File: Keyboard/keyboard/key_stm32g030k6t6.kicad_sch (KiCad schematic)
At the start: 9 parts, among them J1 Conn_01x06_Male, J2 Conn_01x06_Male, SW1 SW_Push, U1 STM32G030K6T6

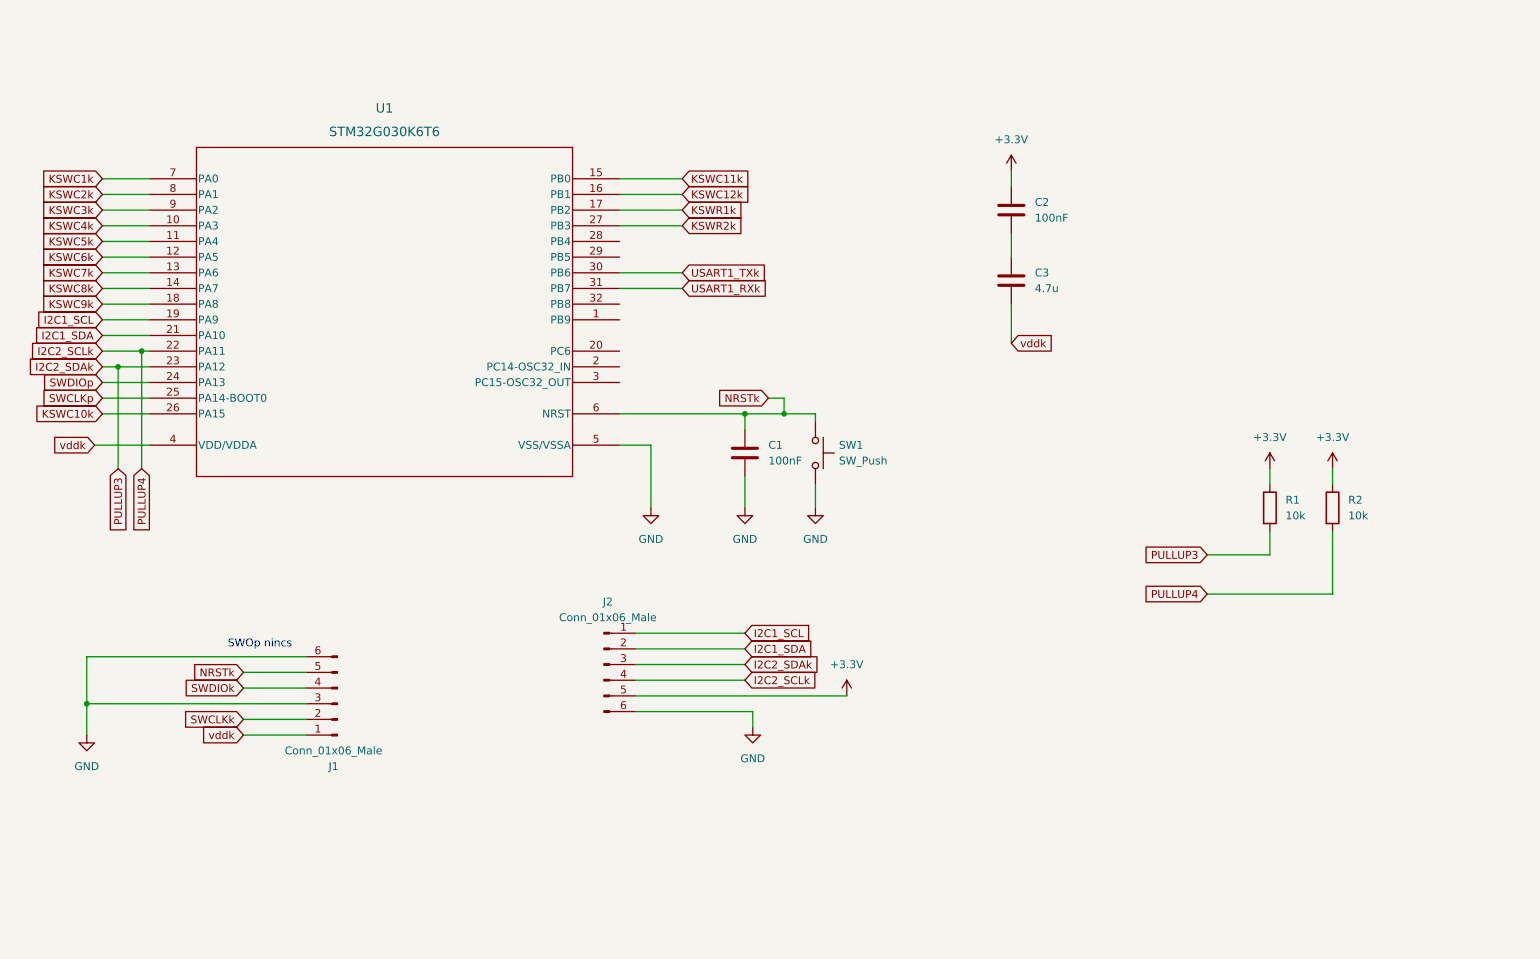
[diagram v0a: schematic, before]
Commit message: fixing keyboard and pot project schematics
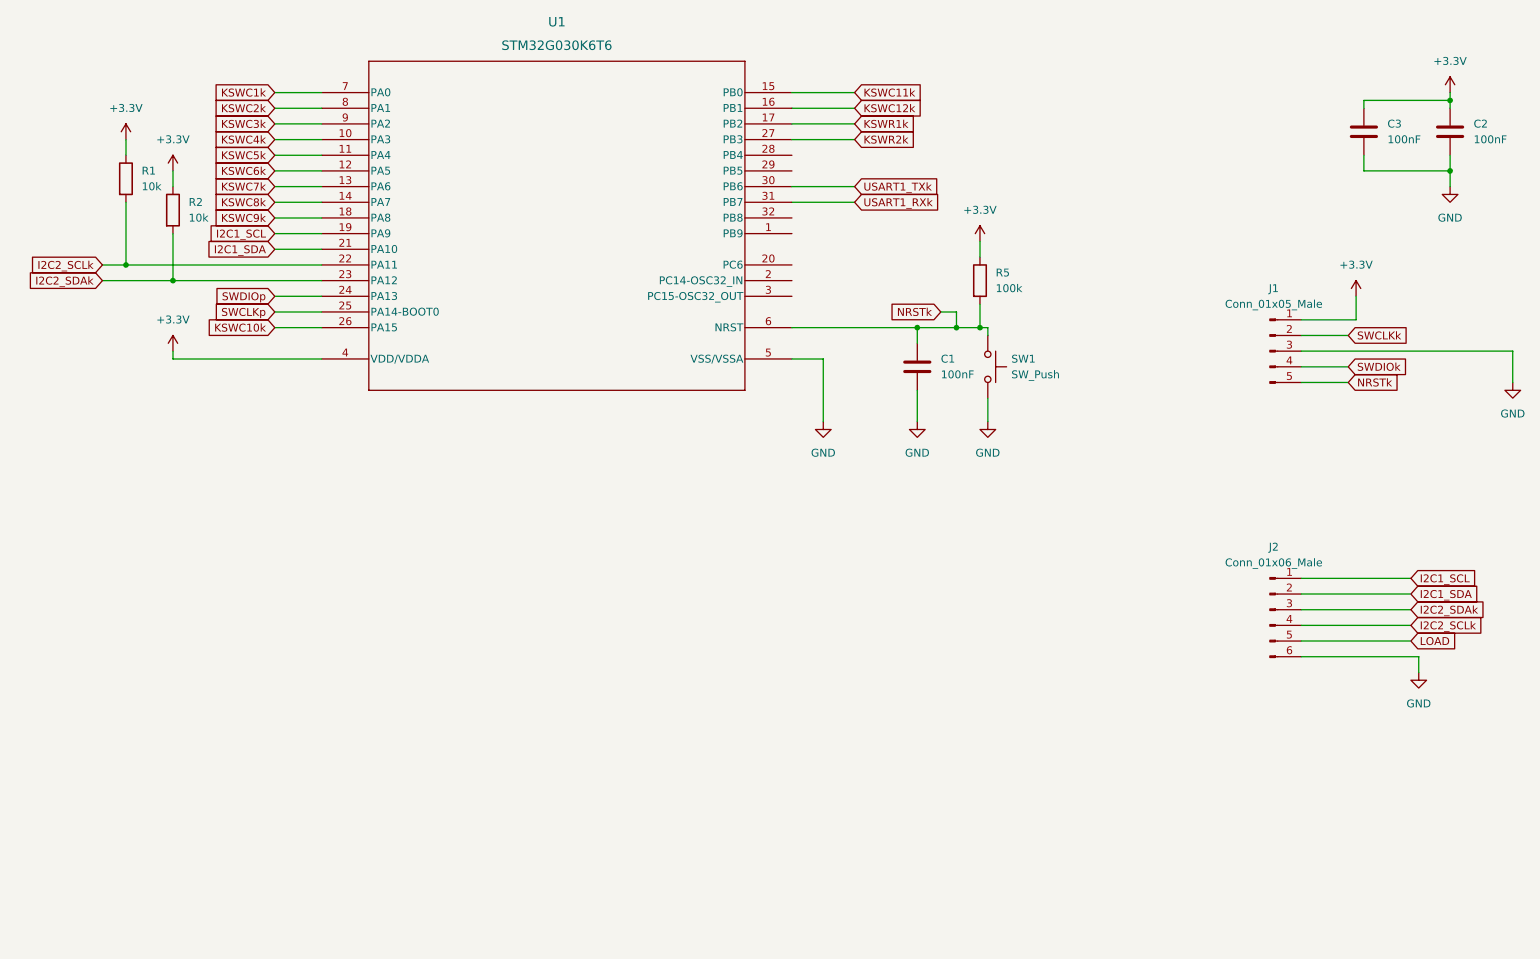
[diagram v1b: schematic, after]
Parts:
- removed J1: Conn_01x06_Male, Connector_PinSocket_2.54mm:PinSocket_1x06_P2.54mm_Horizontal, symbol Connector:Conn_01x06_Male
- added J1: Conn_01x05_Male, symbol Connector:Conn_01x05_Male
- added R5: 100k, Resistor_SMD:R_0805_2012Metric_Pad1.20x1.40mm_HandSolder, symbol Device:R
- C3: value 4.7u -> 100nF
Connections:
- net +3V3: now also C3.1, U1.4 (VDD/VDDA), J1.1 (Pin_1), R5.1; no longer J2.5 (Pin_5)
- net GND: now also C2.2, C3.2, J1.3 (Pin_3)
- net I2C2_SCLk: now also R1.2; no longer R2.2
- net I2C2_SDAk: now also R2.2; no longer R1.2
- net NRSTk: now also J1.5 (Pin_5), R5.2
- net SWCLKk: now also J1.2 (Pin_2)
- net SWDIOk: now also J1.4 (Pin_4)
- removed net vddk: C3.2, U1.4 (VDD/VDDA)
- new net LOAD: J2.5 (Pin_5)
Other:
- note removed: "SWOp nincs"
- moved on the sheet: C1, C2, J2, R1, R2, SW1, U1

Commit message: main_func pcb done
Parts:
- added D14: GREEN LED, LED_SMD:LED_0805_2012Metric_Pad1.15x1.40mm_HandSolder, symbol Device:LED
- added D15: RED LED, LED_SMD:LED_0805_2012Metric_Pad1.15x1.40mm_HandSolder, symbol Device:LED
- added R10, R9: 1k, Resistor_SMD:R_0805_2012Metric_Pad1.20x1.40mm_HandSolder, symbol Device:R
- J1: footprint (none) -> Connector_PinSocket_2.54mm:PinSocket_1x05_P2.54mm_Horizontal
- J2: footprint (none) -> Connector_PinSocket_2.54mm:PinSocket_1x06_P2.54mm_Horizontal
- SW1: footprint (none) -> tactile_button:ROCPU Switches TP10721645
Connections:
- net +3V3: now also D14.2 (A)
- net GND: now also D15.1 (K)
- net USART1_TXk: now also R10.1, R9.1
- new net: D14.1 (K), R9.2
- new net: D15.2 (A), R10.2
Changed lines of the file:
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@@
   (junction (at 173.99 76.2) (diameter 0) (color 0 0 0 0)
   )
+  (junction (at 179.07 113.03) (diameter 0) (color 0 0 0 0)
+  )
   (junction (at 260.35 39.37) (diameter 0) (color 0 0 0 0)
   )
@@
     (stroke (width 0) (type default) (color 0 0 0 0))
   )
+  (wire (pts (xy 179.07 113.03) (xy 161.29 113.03))
+    (stroke (width 0) (type default) (color 0 0 0 0))
+  )
   (wire (pts (xy 173.99 78.74) (xy 173.99 76.2))
     (stroke (width 0) (type default) (color 0 0 0 0))
@@
     (stroke (width 0) (type default) (color 0 0 0 0))
   )
+  (wire (pts (xy 179.07 113.03) (xy 179.07 116.84))
+    (stroke (width 0) (type default) (color 0 0 0 0))
+  )
   (wire (pts (xy 45.72 45.72) (xy 45.72 48.26))
     (stroke (width 0) (type default) (color 0 0 0 0))
   )
+  (wire (pts (xy 179.07 124.46) (xy 179.07 129.54))
+    (stroke (width 0) (type default) (color 0 0 0 0))
+  )
   (wire (pts (xy 180.34 76.2) (xy 173.99 76.2))
     (stroke (width 0) (type default) (color 0 0 0 0))
@@
     (stroke (width 0) (type default) (color 0 0 0 0))
   )
+  (wire (pts (xy 186.69 113.03) (xy 179.07 113.03))
+    (stroke (width 0) (type default) (color 0 0 0 0))
+  )
   (wire (pts (xy 236.22 121.92) (xy 254 121.92))
     (stroke (width 0) (type default) (color 0 0 0 0))
@@
     (stroke (width 0) (type default) (color 0 0 0 0))
   )
+  (wire (pts (xy 156.21 146.05) (xy 161.29 146.05))
+    (stroke (width 0) (type default) (color 0 0 0 0))
+  )
   (wire (pts (xy 246.38 48.26) (xy 246.38 50.8))
     (stroke (width 0) (type default) (color 0 0 0 0))
@@
     (stroke (width 0) (type default) (color 0 0 0 0))
   )
+  (wire (pts (xy 161.29 113.03) (xy 161.29 116.84))
+    (stroke (width 0) (type default) (color 0 0 0 0))
+  )
   (wire (pts (xy 69.85 45.72) (xy 77.47 45.72))
     (stroke (width 0) (type default) (color 0 0 0 0))
@@
     (stroke (width 0) (type default) (color 0 0 0 0))
   )
+  (wire (pts (xy 179.07 137.16) (xy 179.07 144.78))
+    (stroke (width 0) (type default) (color 0 0 0 0))
+  )
   (wire (pts (xy 236.22 124.46) (xy 254 124.46))
     (stroke (width 0) (type default) (color 0 0 0 0))
@@
     (stroke (width 0) (type default) (color 0 0 0 0))
   )
+  (wire (pts (xy 156.21 143.51) (xy 156.21 146.05))
+    (stroke (width 0) (type default) (color 0 0 0 0))
+  )
   (wire (pts (xy 153.67 38.1) (xy 163.83 38.1))
     (stroke (width 0) (type default) (color 0 0 0 0))
@@
     (stroke (width 0) (type default) (color 0 0 0 0))
   )
+  (wire (pts (xy 161.29 124.46) (xy 161.29 129.54))
+    (stroke (width 0) (type default) (color 0 0 0 0))
+  )
   (wire (pts (xy 260.35 48.26) (xy 260.35 50.8))
     (stroke (width 0) (type default) (color 0 0 0 0))
@@
     (stroke (width 0) (type default) (color 0 0 0 0))
   )
+  (wire (pts (xy 161.29 146.05) (xy 161.29 137.16))
+    (stroke (width 0) (type default) (color 0 0 0 0))
+  )
   (wire (pts (xy 41.91 68.58) (xy 53.34 68.58))
     (stroke (width 0) (type default) (color 0 0 0 0))
@@
     (property "Intersheet References" "${INTERSHEET_REFS}" (id 0) (at 59.9983 38.0206 0)
       (effects (font (size 1.27 1.27)) (justify right) hide)
+    )
+  )
+  (global_label "USART1_TXk" (shape input) (at 186.69 113.03 0) (fields_autoplaced)
+    (effects (font (size 1.27 1.27)) (justify left))
+    (property "Intersheet References" "${INTERSHEET_REFS}" (id 0) (at 200.3517 112.9506 0)
+      (effects (font (size 1.27 1.27)) (justify left) hide)
     )
   )
@@
     (pin "1")
   )
+  (symbol (lib_id "Device:R") (at 161.29 120.65 0) (unit 1)
+    (in_bom yes) (on_board yes) (fields_autoplaced)
+    (property "Reference" "R9" (id 0) (at 163.83 119.3799 0)
+      (effects (font (size 1.27 1.27)) (justify left))
+    )
+    (property "Value" "1k" (id 1) (at 163.83 121.9199 0)
+      (effects (font (size 1.27 1.27)) (justify left))
+    )
+    (property "Footprint" "Resistor_SMD:R_0805_2012Metric_Pad1.20x1.40mm_HandSolder" (id 2) (at 159.512 120.65 90)
+      (effects (font (size 1.27 1.27)) hide)
+    )
+    (property "Datasheet" "~" (id 3) (at 161.29 120.65 0)
+      (effects (font (size 1.27 1.27)) hide)
+    )
+    (pin "1")
+    (pin "2")
+  )
   (symbol (lib_id "power:GND") (at 255.27 132.08 0) (unit 1)
     (in_bom yes) (on_board yes) (fields_autoplaced)
@@
     (pin "1")
   )
+  (symbol (lib_id "Device:R") (at 179.07 120.65 0) (unit 1)
+    (in_bom yes) (on_board yes) (fields_autoplaced)
+    (property "Reference" "R10" (id 0) (at 181.61 119.3799 0)
+      (effects (font (size 1.27 1.27)) (justify left))
+    )
+    (property "Value" "1k" (id 1) (at 181.61 121.9199 0)
+      (effects (font (size 1.27 1.27)) (justify left))
+    )
+    (property "Footprint" "Resistor_SMD:R_0805_2012Metric_Pad1.20x1.40mm_HandSolder" (id 2) (at 177.292 120.65 90)
+      (effects (font (size 1.27 1.27)) hide)
+    )
+    (property "Datasheet" "~" (id 3) (at 179.07 120.65 0)
+      (effects (font (size 1.27 1.27)) hide)
+    )
+    (pin "1")
+    (pin "2")
+  )
   (symbol (lib_id "Device:R") (at 53.34 57.15 0) (unit 1)
     (in_bom yes) (on_board yes) (fields_autoplaced)
@@
     (property "Reference" "J2" (id 0) (at 231.775 111.76 0))
     (property "Value" "Conn_01x06_Male" (id 1) (at 231.775 114.3 0))
-    (property "Footprint" "" (id 2) (at 231.14 121.92 0)
+    (property "Footprint" "Connector_PinSocket_2.54mm:PinSocket_1x06_P2.54mm_Horizontal" (id 2) (at 231.14 121.92 0)
       (effects (font (size 1.27 1.27)) hide)
     )
@@
     (pin "1")
   )
+  (symbol (lib_id "power:+3.3V") (at 156.21 143.51 0) (unit 1)
+    (in_bom yes) (on_board yes) (fields_autoplaced)
+    (property "Reference" "#PWR016" (id 0) (at 156.21 147.32 0)
+      (effects (font (size 1.27 1.27)) hide)
+    )
+    (property "Value" "+3.3V" (id 1) (at 156.21 138.43 0))
+    (property "Footprint" "" (id 2) (at 156.21 143.51 0)
+      (effects (font (size 1.27 1.27)) hide)
+    )
+    (property "Datasheet" "" (id 3) (at 156.21 143.51 0)
+      (effects (font (size 1.27 1.27)) hide)
+    )
+    (pin "1")
+  )
   (symbol (lib_id "power:+3.3V") (at 53.34 50.8 0) (unit 1)
     (in_bom yes) (on_board yes) (fields_autoplaced)
@@
     (pin "1")
   )
+  (symbol (lib_id "Device:LED") (at 179.07 133.35 90) (unit 1)
+    (in_bom yes) (on_board yes) (fields_autoplaced)
+    (property "Reference" "D15" (id 0) (at 182.88 133.6674 90)
+      (effects (font (size 1.27 1.27)) (justify right))
+    )
+    (property "Value" "RED LED" (id 1) (at 182.88 136.2074 90)
+      (effects (font (size 1.27 1.27)) (justify right))
+    )
+    (property "Footprint" "LED_SMD:LED_0805_2012Metric_Pad1.15x1.40mm_HandSolder" (id 2) (at 179.07 133.35 0)
+      (effects (font (size 1.27 1.27)) hide)
+    )
+    (property "Datasheet" "~" (id 3) (at 179.07 133.35 0)
+      (effects (font (size 1.27 1.27)) hide)
+    )
+    (pin "1")
+    (pin "2")
+  )
   (symbol (lib_id "Connector:Conn_01x05_Male") (at 231.14 80.01 0) (unit 1)
     (in_bom yes) (on_board yes) (fields_autoplaced)
     (property "Reference" "J1" (id 0) (at 231.775 69.85 0))
     (property "Value" "Conn_01x05_Male" (id 1) (at 231.775 72.39 0))
-    (property "Footprint" "" (id 2) (at 231.14 80.01 0)
+    (property "Footprint" "Connector_PinSocket_2.54mm:PinSocket_1x05_P2.54mm_Horizontal" (id 2) (at 231.14 80.01 0)
       (effects (font (size 1.27 1.27)) hide)
     )
@@
     )
     (pin "1")
+  )
+  (symbol (lib_id "Device:LED") (at 161.29 133.35 270) (unit 1)
+    (in_bom yes) (on_board yes) (fields_autoplaced)
+    (property "Reference" "D14" (id 0) (at 163.83 130.4924 90)
+      (effects (font (size 1.27 1.27)) (justify left))
+    )
+    (property "Value" "GREEN LED" (id 1) (at 163.83 133.0324 90)
+      (effects (font (size 1.27 1.27)) (justify left))
+    )
+    (property "Footprint" "LED_SMD:LED_0805_2012Metric_Pad1.15x1.40mm_HandSolder" (id 2) (at 161.29 133.35 0)
+      (effects (font (size 1.27 1.27)) hide)
+    )
+    (property "Datasheet" "~" (id 3) (at 161.29 133.35 0)
+      (effects (font (size 1.27 1.27)) hide)
+    )
+    (pin "1")
+    (pin "2")
   )
   (symbol (lib_id "2023-04-19_13-34-55:STM32G030K6T6") (at 77.47 38.1 0) (unit 1)
@@
       (effects (font (size 1.27 1.27)) (justify left))
     )
-    (property "Footprint" "" (id 2) (at 190.5 82.55 0)
+    (property "Footprint" "tactile_button:ROCPU Switches TP10721645" (id 2) (at 190.5 82.55 0)
       (effects (font (size 1.27 1.27)) hide)
     )
@@
     (pin "2")
   )
+  (symbol (lib_id "power:GND") (at 179.07 144.78 0) (unit 1)
+    (in_bom yes) (on_board yes) (fields_autoplaced)
+    (property "Reference" "#PWR017" (id 0) (at 179.07 151.13 0)
+      (effects (font (size 1.27 1.27)) hide)
+    )
+    (property "Value" "GND" (id 1) (at 179.07 149.86 0))
+    (property "Footprint" "" (id 2) (at 179.07 144.78 0)
+      (effects (font (size 1.27 1.27)) hide)
+    )
+    (property "Datasheet" "" (id 3) (at 179.07 144.78 0)
+      (effects (font (size 1.27 1.27)) hide)
+    )
+    (pin "1")
+  )
   (symbol (lib_id "Device:C") (at 246.38 44.45 0) (unit 1)

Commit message: PCB designs done v1
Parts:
- added J3: Conn_01x06_Male, Connector_PinSocket_2.54mm:PinSocket_1x06_P2.54mm_Vertical, symbol Connector:Conn_01x06_Male
- J1: footprint Connector_PinSocket_2.54mm:PinSocket_1x05_P2.54mm_Horizontal -> Connector_PinSocket_2.54mm:PinSocket_1x05_P2.54mm_Vertical
- J2: footprint Connector_PinSocket_2.54mm:PinSocket_1x06_P2.54mm_Horizontal -> Connector_PinSocket_2.54mm:PinSocket_1x06_P2.54mm_Vertical
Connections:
- net SWCLKp is gone; now on net SWCLKk: U1.25 (PA14-BOOT0)
- net SWDIOp is gone; now on net SWDIOk: U1.24 (PA13)
- net GND: now also J3.6 (Pin_6)
- net I2C1_SCL: now also J3.1 (Pin_1)
- net I2C1_SDA: now also J3.2 (Pin_2)
- net I2C2_SCLk: now also J3.4 (Pin_4)
- net I2C2_SDAk: now also J3.3 (Pin_3)
- net KSWC10k: now also U1.17 (PB2); no longer U1.26 (PA15)
- net KSWC11k: now also U1.18 (PA8); no longer U1.15 (PB0)
- net KSWC12k: now also U1.20 (PC6); no longer U1.16 (PB1)
- net KSWC1k: now also U1.8 (PA1); no longer U1.7 (PA0)
- net KSWC2k: now also U1.9 (PA2); no longer U1.8 (PA1)
- net KSWC3k: now also U1.10 (PA3); no longer U1.9 (PA2)
- net KSWC4k: now also U1.11 (PA4); no longer U1.10 (PA3)
- net KSWC5k: now also U1.12 (PA5); no longer U1.11 (PA4)
- net KSWC6k: now also U1.13 (PA6); no longer U1.12 (PA5)
- net KSWC7k: now also U1.14 (PA7); no longer U1.13 (PA6)
- net KSWC8k: now also U1.15 (PB0); no longer U1.14 (PA7)
- net KSWC9k: now also U1.16 (PB1); no longer U1.18 (PA8)
- net KSWR1k: now also U1.7 (PA0); no longer U1.17 (PB2)
- net LOAD: now also J3.5 (Pin_5)
- net KSWR2k: no longer names the net of U1.27 (PB3)
- net USART1_RXk: no longer names the net of U1.31 (PB7)

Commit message: pcb design fixing
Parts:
- removed C3: 100nF, Capacitor_SMD:C_0805_2012Metric_Pad1.18x1.45mm_HandSolder, symbol Device:C
- removed D14: GREEN LED, LED_SMD:LED_0805_2012Metric_Pad1.15x1.40mm_HandSolder, symbol Device:LED
- removed D15: RED LED, LED_SMD:LED_0805_2012Metric_Pad1.15x1.40mm_HandSolder, symbol Device:LED
- removed J2, J3: Conn_01x06_Male, Connector_PinSocket_2.54mm:PinSocket_1x06_P2.54mm_Vertical, symbol Connector:Conn_01x06_Male
- removed R10, R9: 1k, Resistor_SMD:R_0805_2012Metric_Pad1.20x1.40mm_HandSolder, symbol Device:R
- added D1: GREEN LED, LED_SMD:LED_0805_2012Metric_Pad1.15x1.40mm_HandSolder, symbol Device:LED
- added D2: RED LED, LED_SMD:LED_0805_2012Metric_Pad1.15x1.40mm_HandSolder, symbol Device:LED
- added J2, J3, J4: Conn_01x10_Male, Connector_IDC:IDC-Header_2x05_P2.54mm_Horizontal, symbol Connector:Conn_01x10_Male
- added R3, R4: 1k, Resistor_SMD:R_0805_2012Metric_Pad1.20x1.40mm_HandSolder, symbol Device:R
- R5: value 100k -> 10k
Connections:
- net KSWR1k is gone; now on net KSWC1k: U1.7 (PA0)
- net GND: now also D1.1 (K), D2.1 (K), J2.10 (Pin_10), J2.2 (Pin_2), J2.4 (Pin_4), J2.6 (Pin_6), J2.8 (Pin_8), J2.9 (Pin_9), J3.1 (Pin_1), J3.10 (Pin_10), J3.2 (Pin_2), J3.4 (Pin_4), J3.6 (Pin_6), J3.8 (Pin_8), J4.1 (Pin_1), J4.10 (Pin_10), J4.2 (Pin_2), J4.4 (Pin_4), J4.6 (Pin_6), J4.8 (Pin_8)
- net I2C1_SCL: now also J2.7 (Pin_7)
- net I2C1_SDA: now also J2.5 (Pin_5)
- net I2C2_SCLk: now also J3.5 (Pin_5), J4.5 (Pin_5)
- net I2C2_SDAk: now also J3.3 (Pin_3), J4.3 (Pin_3)
- net KSWC10k: now also U1.16 (PB1); no longer U1.17 (PB2)
- net KSWC11k: now also U1.17 (PB2); no longer U1.18 (PA8)
- net KSWC12k: now also U1.18 (PA8); no longer U1.20 (PC6)
- net KSWC1k: no longer U1.8 (PA1)
- net KSWC2k: now also U1.8 (PA1); no longer U1.9 (PA2)
- net KSWC3k: now also U1.9 (PA2); no longer U1.10 (PA3)
- net KSWC4k: now also U1.10 (PA3); no longer U1.11 (PA4)
- net KSWC5k: now also U1.11 (PA4); no longer U1.12 (PA5)
- net KSWC6k: now also U1.12 (PA5); no longer U1.13 (PA6)
- net KSWC7k: now also U1.13 (PA6); no longer U1.14 (PA7)
- net KSWC8k: now also U1.14 (PA7); no longer U1.15 (PB0)
- net KSWC9k: now also U1.15 (PB0); no longer U1.16 (PB1)
- net LOAD: now also J2.1 (Pin_1), J2.3 (Pin_3), J3.7 (Pin_7), J3.9 (Pin_9), J4.7 (Pin_7), J4.9 (Pin_9), R3.1
- net USART1_TXk renamed STATUS_LEDk
- net STATUS_LEDk: now also R4.1
- new net: D1.2 (A), R3.2
- new net: D2.2 (A), R4.2
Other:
- moved on the sheet: C2

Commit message: gerber files generated
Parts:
- J3, J4: footprint Connector_IDC:IDC-Header_2x05_P2.54mm_Horizontal -> Connector_IDC:IDC-Header_2x05_P2.54mm_Vertical
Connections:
- net GND: now also J3.9 (Pin_9), J4.9 (Pin_9); no longer J3.1 (Pin_1), J4.1 (Pin_1)
- net I2C2_SDAk: now also J3.7 (Pin_7), J4.7 (Pin_7); no longer J3.3 (Pin_3), J4.3 (Pin_3)
- net LOAD: now also J3.1 (Pin_1), J3.3 (Pin_3), J4.1 (Pin_1), J4.3 (Pin_3); no longer J3.7 (Pin_7), J3.9 (Pin_9), J4.7 (Pin_7), J4.9 (Pin_9)
